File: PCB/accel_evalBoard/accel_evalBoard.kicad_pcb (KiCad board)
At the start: 2 copper layers, 9 parts, among them J1 Conn_02x03_Odd_Even

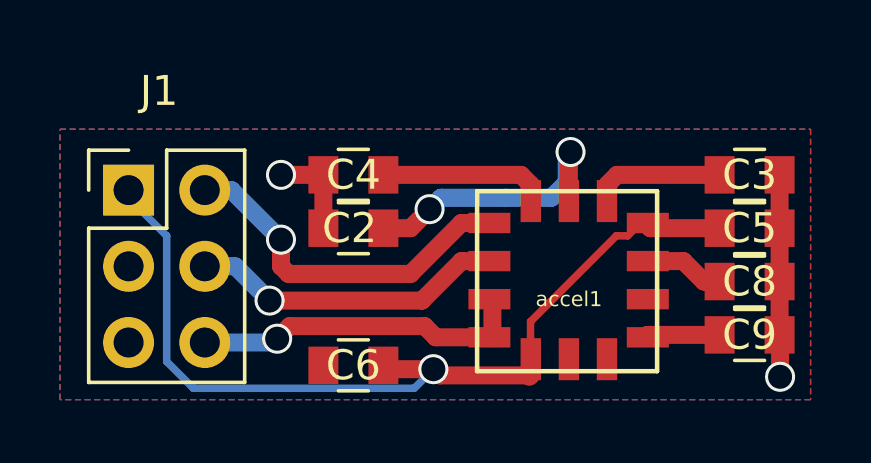
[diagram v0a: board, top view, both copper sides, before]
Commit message: Update ground plan & connexion to accel
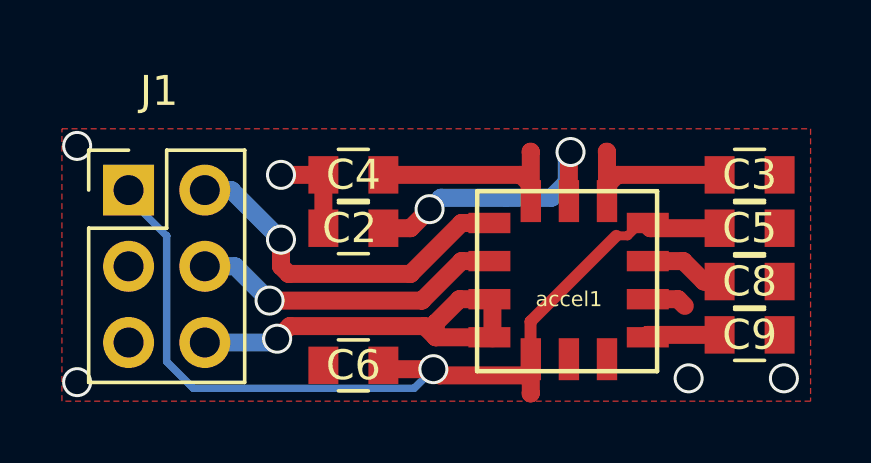
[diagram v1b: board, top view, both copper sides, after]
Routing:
- net GNDREF: track 9.93 -> 4.61 mm, vias 2 -> 5
- net Net-(J1-Pad6): track 11.2 -> 14.0 mm
- net Net-(C4-Pad1): track 5.06 -> 6.17 mm
- net Net-(C3-Pad1): track 3.89 -> 5.00 mm
- net VDD: track 30.4 -> 31.0 mm
- removed copper zone on B.Cu, net GNDREF

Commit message: Update ground plan & connexion to accel
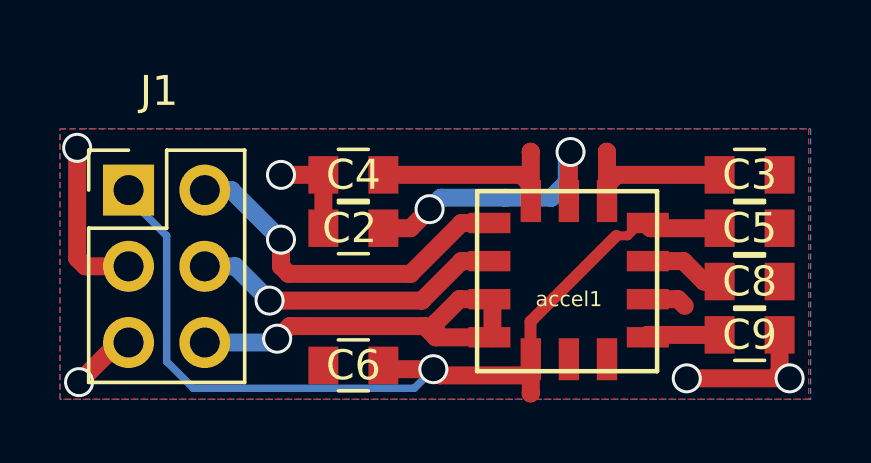
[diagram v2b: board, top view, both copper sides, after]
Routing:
- net GNDREF: track 4.61 -> 17.4 mm
- added copper zone on B.Cu, net GNDREF
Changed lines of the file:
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@@
   (general
     (links 24)
-    (no_connects 1)
+    (no_connects 0)
     (area 160.265 61.5352 199.373715 79.150201)
     (thickness 1.6)
     (drawings 10)
-    (tracks 83)
+    (tracks 92)
     (zones 0)
     (modules 9)
@@
   (gr_line (start 188.746 72.8472) (end 163.746 72.8472) (angle 90) (layer F.Fab) (width 0.2))
   (gr_line (start 188.73 63.873) (end 188.73 72.873) (angle 90) (layer F.Fab) (width 0.2))
-  (via (at 164.2745 64.389) (size 1) (drill 0.8) (layers F.Cu B.Cu) (net 1))
-  (via (at 164.2745 72.263) (size 1) (drill 0.8) (layers F.Cu B.Cu) (net 1))
-  (via (at 184.658 72.136) (size 1) (drill 0.8) (layers F.Cu B.Cu) (net 1))
-  (via (at 187.833 72.136) (size 1) (drill 0.8) (layers F.Cu B.Cu) (net 1))
+  (segment (start 165.989 68.4022) (end 164.5412 68.4022) (width 0.6) (layer F.Cu) (net 1) (status 400000))
+  (via (at 164.2745 64.4525) (size 1) (drill 0.8) (layers F.Cu B.Cu) (net 1))
+  (segment (start 164.2745 68.1355) (end 164.2745 64.4525) (width 0.6) (layer F.Cu) (net 1))
+  (segment (start 164.5412 68.4022) (end 164.2745 68.1355) (width 0.6) (layer F.Cu) (net 1))
+  (segment (start 165.989 70.9422) (end 165.6588 70.9422) (width 0.6) (layer F.Cu) (net 1) (status C00000))
+  (segment (start 165.6588 70.9422) (end 164.338 72.263) (width 0.6) (layer F.Cu) (net 1) (status 400000))
+  (via (at 164.338 72.263) (size 1) (drill 0.8) (layers F.Cu B.Cu) (net 1))
+  (segment (start 184.5945 72.136) (end 188.0235 72.136) (width 0.6) (layer F.Cu) (net 1))
+  (segment (start 187.69 71.866) (end 187.96 72.136) (width 0.6) (layer F.Cu) (net 1))
+  (segment (start 187.96 72.136) (end 188.0235 72.136) (width 0.6) (layer F.Cu) (net 1))
+  (via (at 188.0235 72.136) (size 1) (drill 0.8) (layers F.Cu B.Cu) (net 1))
+  (segment (start 187.69 71.866) (end 187.69 70.6882) (width 0.6) (layer F.Cu) (net 1) (status 800000))
+  (via (at 184.5945 72.136) (size 1) (drill 0.8) (layers F.Cu B.Cu) (net 1))
   (segment (start 183.206 69.4982) (end 184.3062 69.4982) (width 0.6) (layer F.Cu) (net 1))
   (segment (start 184.3062 69.4982) (end 184.531 69.723) (width 0.6) (layer F.Cu) (net 1))
@@
   (segment (start 179.396 65.6802) (end 179.07 65.3542) (width 0.6) (layer F.Cu) (net 10))
   (segment (start 179.07 65.3542) (end 174.482 65.3542) (width 0.6) (layer F.Cu) (net 10))
+  (zone (net 1) (net_name GNDREF) (layer B.Cu) (hatch edge 0.508)
+    (connect_pads yes (clearance 0.508))
+    (min_thickness 0.254)
+    (fill yes (arc_segments 16) (thermal_gap 0.508) (thermal_bridge_width 0.508))
+    (polygon
+      (pts
+        (xy 188.722 72.8345) (xy 163.703 72.8345) (xy 163.703 63.8175) (xy 188.722 63.8175)
+      )
+    )
+  )
   (zone (net 1) (net_name GNDREF) (layer F.Cu) (hatch edge 0.508)
     (connect_pads yes (clearance 0.508))
@@
     (polygon
       (pts
-        (xy 188.722 72.898) (xy 163.7665 72.898) (xy 163.7665 63.8175) (xy 188.722 63.8175)
+        (xy 164.4015 63.8175) (xy 188.6585 63.8175) (xy 188.6585 72.8345) (xy 163.703 72.8345) (xy 163.703 63.8175)
       )
     )
